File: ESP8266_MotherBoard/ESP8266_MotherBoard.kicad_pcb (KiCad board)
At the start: 2 copper layers, 67 parts, among them CN1 DIP-BLACK-FEMALE-HEADER-VERT_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, IC1 ADXL345, J1 Screw_Terminal_01x03, J10 Screw_Terminal_01x06, J11 Screw_Terminal_01x12, J2 DIP-BLACK-MALE-HEADER-VERT_4P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, J3 Screw_Terminal_01x02, J5 DIP-BLACK-MALE-HEADER-R_A_3P-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, J6 Screw_Terminal_01x02, J7 DIP-BLACK-MALE-HEADER-R_A_3P-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

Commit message: test branch sch and board changed
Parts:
- removed D5: 1N4001, OPL_Discrete_Semiconductor:DO-41
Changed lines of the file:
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@@
     (tracks 0)
     (zones 0)
-    (modules 67)
+    (modules 66)
     (nets 91)
   )
@@
       (net 38 GND))
   )
-  (module OPL_Discrete_Semiconductor:DO-41 (layer F.Cu)
-    (at 254 184.15 180)
-    (attr virtual)
-    (fp_text reference D5 (at 0 -2.286 180) (layer F.SilkS)
-      (effects (font (size 1 1) (thickness 0.15)))
-    )
-    (fp_text value 1N4001 (at 0 2.275 180) (layer F.Fab)
-      (effects (font (size 1 1) (thickness 0.15)))
-    )
-    (fp_line (start -2.54 -1.27) (end 2.54 -1.27) (layer F.SilkS) (width 0.127))
-    (fp_line (start -2.54 1.27) (end -2.54 -1.27) (layer F.SilkS) (width 0.127))
-    (fp_line (start 2.54 1.27) (end -2.54 1.27) (layer F.SilkS) (width 0.127))
-    (fp_line (start 2.54 -1.27) (end 2.54 1.27) (layer F.SilkS) (width 0.127))
-    (fp_line (start 2.54 0.3175) (end 2.54 -0.3175) (layer F.SilkS) (width 0.06604))
-    (fp_line (start 2.54 -0.3175) (end 3.29946 -0.3175) (layer F.SilkS) (width 0.06604))
-    (fp_line (start 3.29946 0.3175) (end 3.29946 -0.3175) (layer F.SilkS) (width 0.06604))
-    (fp_line (start 2.54 0.3175) (end 3.29946 0.3175) (layer F.SilkS) (width 0.06604))
-    (fp_line (start -3.29946 0.3175) (end -3.29946 -0.3175) (layer F.SilkS) (width 0.06604))
-    (fp_line (start -3.29946 -0.3175) (end -2.54 -0.3175) (layer F.SilkS) (width 0.06604))
-    (fp_line (start -2.54 0.3175) (end -2.54 -0.3175) (layer F.SilkS) (width 0.06604))
-    (fp_line (start -3.29946 0.3175) (end -2.54 0.3175) (layer F.SilkS) (width 0.06604))
-    (fp_line (start 1.27 1.27) (end 1.27 -1.27) (layer F.SilkS) (width 0.06604))
-    (fp_line (start 1.27 -1.27) (end 1.905 -1.27) (layer F.SilkS) (width 0.06604))
-    (fp_line (start 1.905 1.27) (end 1.905 -1.27) (layer F.SilkS) (width 0.06604))
-    (fp_line (start 1.27 1.27) (end 1.905 1.27) (layer F.SilkS) (width 0.06604))
-    (fp_line (start -2.325 -1) (end 2.325 -1) (layer F.Fab) (width 0.1))
-    (fp_line (start 2.325 -1) (end 2.325 1) (layer F.Fab) (width 0.1))
-    (fp_line (start 2.325 1) (end -2.325 1) (layer F.Fab) (width 0.1))
-    (fp_line (start -2.325 1) (end -2.325 -1) (layer F.Fab) (width 0.1))
-    (fp_line (start 5.65 -1.2) (end -5.65 -1.2) (layer F.CrtYd) (width 0.05))
-    (fp_line (start -5.65 -1.2) (end -5.65 1.2) (layer F.CrtYd) (width 0.05))
-    (fp_line (start -5.65 1.2) (end 5.65 1.2) (layer F.CrtYd) (width 0.05))
-    (fp_line (start 5.65 1.2) (end 5.65 -1.2) (layer F.CrtYd) (width 0.05))
-    (fp_text user %R (at 0 0 180) (layer F.Fab)
-      (effects (font (size 1 1) (thickness 0.15)))
-    )
-    (pad 2 thru_hole circle (at 4.445 0 180) (size 1.905 1.905) (drill 1.0414) (layers *.Cu *.Mask)
-      (net 38 GND))
-    (pad 1 thru_hole circle (at -4.445 0 180) (size 1.905 1.905) (drill 1.0414) (layers *.Cu *.Mask)
-      (net 36 PWM__toLoad_1))
-  )
   (module OPL_Discrete_Semiconductor:SOT-23 (layer F.Cu)

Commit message: added D3 ro PWM modul
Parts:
- added D3: 1N4001, OPL_Discrete_Semiconductor:DO-41, F.Cu at (250.2, 184.8)
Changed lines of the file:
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@@
     (tracks 0)
     (zones 0)
-    (modules 66)
+    (modules 67)
     (nets 91)
   )
@@
     )
   )
+  (module OPL_Discrete_Semiconductor:DO-41 (layer F.Cu)
+    (at 250.19 184.785)
+    (attr virtual)
+    (fp_text reference D3 (at 0 -2.286) (layer F.SilkS)
+      (effects (font (size 1 1) (thickness 0.15)))
+    )
+    (fp_text value 1N4001 (at 0 2.275) (layer F.Fab)
+      (effects (font (size 1 1) (thickness 0.15)))
+    )
+    (fp_line (start -2.54 -1.27) (end 2.54 -1.27) (layer F.SilkS) (width 0.127))
+    (fp_line (start -2.54 1.27) (end -2.54 -1.27) (layer F.SilkS) (width 0.127))
+    (fp_line (start 2.54 1.27) (end -2.54 1.27) (layer F.SilkS) (width 0.127))
+    (fp_line (start 2.54 -1.27) (end 2.54 1.27) (layer F.SilkS) (width 0.127))
+    (fp_line (start 2.54 0.3175) (end 2.54 -0.3175) (layer F.SilkS) (width 0.06604))
+    (fp_line (start 2.54 -0.3175) (end 3.29946 -0.3175) (layer F.SilkS) (width 0.06604))
+    (fp_line (start 3.29946 0.3175) (end 3.29946 -0.3175) (layer F.SilkS) (width 0.06604))
+    (fp_line (start 2.54 0.3175) (end 3.29946 0.3175) (layer F.SilkS) (width 0.06604))
+    (fp_line (start -3.29946 0.3175) (end -3.29946 -0.3175) (layer F.SilkS) (width 0.06604))
+    (fp_line (start -3.29946 -0.3175) (end -2.54 -0.3175) (layer F.SilkS) (width 0.06604))
+    (fp_line (start -2.54 0.3175) (end -2.54 -0.3175) (layer F.SilkS) (width 0.06604))
+    (fp_line (start -3.29946 0.3175) (end -2.54 0.3175) (layer F.SilkS) (width 0.06604))
+    (fp_line (start 1.27 1.27) (end 1.27 -1.27) (layer F.SilkS) (width 0.06604))
+    (fp_line (start 1.27 -1.27) (end 1.905 -1.27) (layer F.SilkS) (width 0.06604))
+    (fp_line (start 1.905 1.27) (end 1.905 -1.27) (layer F.SilkS) (width 0.06604))
+    (fp_line (start 1.27 1.27) (end 1.905 1.27) (layer F.SilkS) (width 0.06604))
+    (fp_line (start -2.325 -1) (end 2.325 -1) (layer F.Fab) (width 0.1))
+    (fp_line (start 2.325 -1) (end 2.325 1) (layer F.Fab) (width 0.1))
+    (fp_line (start 2.325 1) (end -2.325 1) (layer F.Fab) (width 0.1))
+    (fp_line (start -2.325 1) (end -2.325 -1) (layer F.Fab) (width 0.1))
+    (fp_line (start 5.65 -1.2) (end -5.65 -1.2) (layer F.CrtYd) (width 0.05))
+    (fp_line (start -5.65 -1.2) (end -5.65 1.2) (layer F.CrtYd) (width 0.05))
+    (fp_line (start -5.65 1.2) (end 5.65 1.2) (layer F.CrtYd) (width 0.05))
+    (fp_line (start 5.65 1.2) (end 5.65 -1.2) (layer F.CrtYd) (width 0.05))
+    (fp_text user %R (at 0 0) (layer F.Fab)
+      (effects (font (size 1 1) (thickness 0.15)))
+    )
+    (pad 2 thru_hole circle (at 4.445 0) (size 1.905 1.905) (drill 1.0414) (layers *.Cu *.Mask)
+      (net 38 GND))
+    (pad 1 thru_hole circle (at -4.445 0) (size 1.905 1.905) (drill 1.0414) (layers *.Cu *.Mask)
+      (net 36 PWM__toLoad_1))
+  )
 )

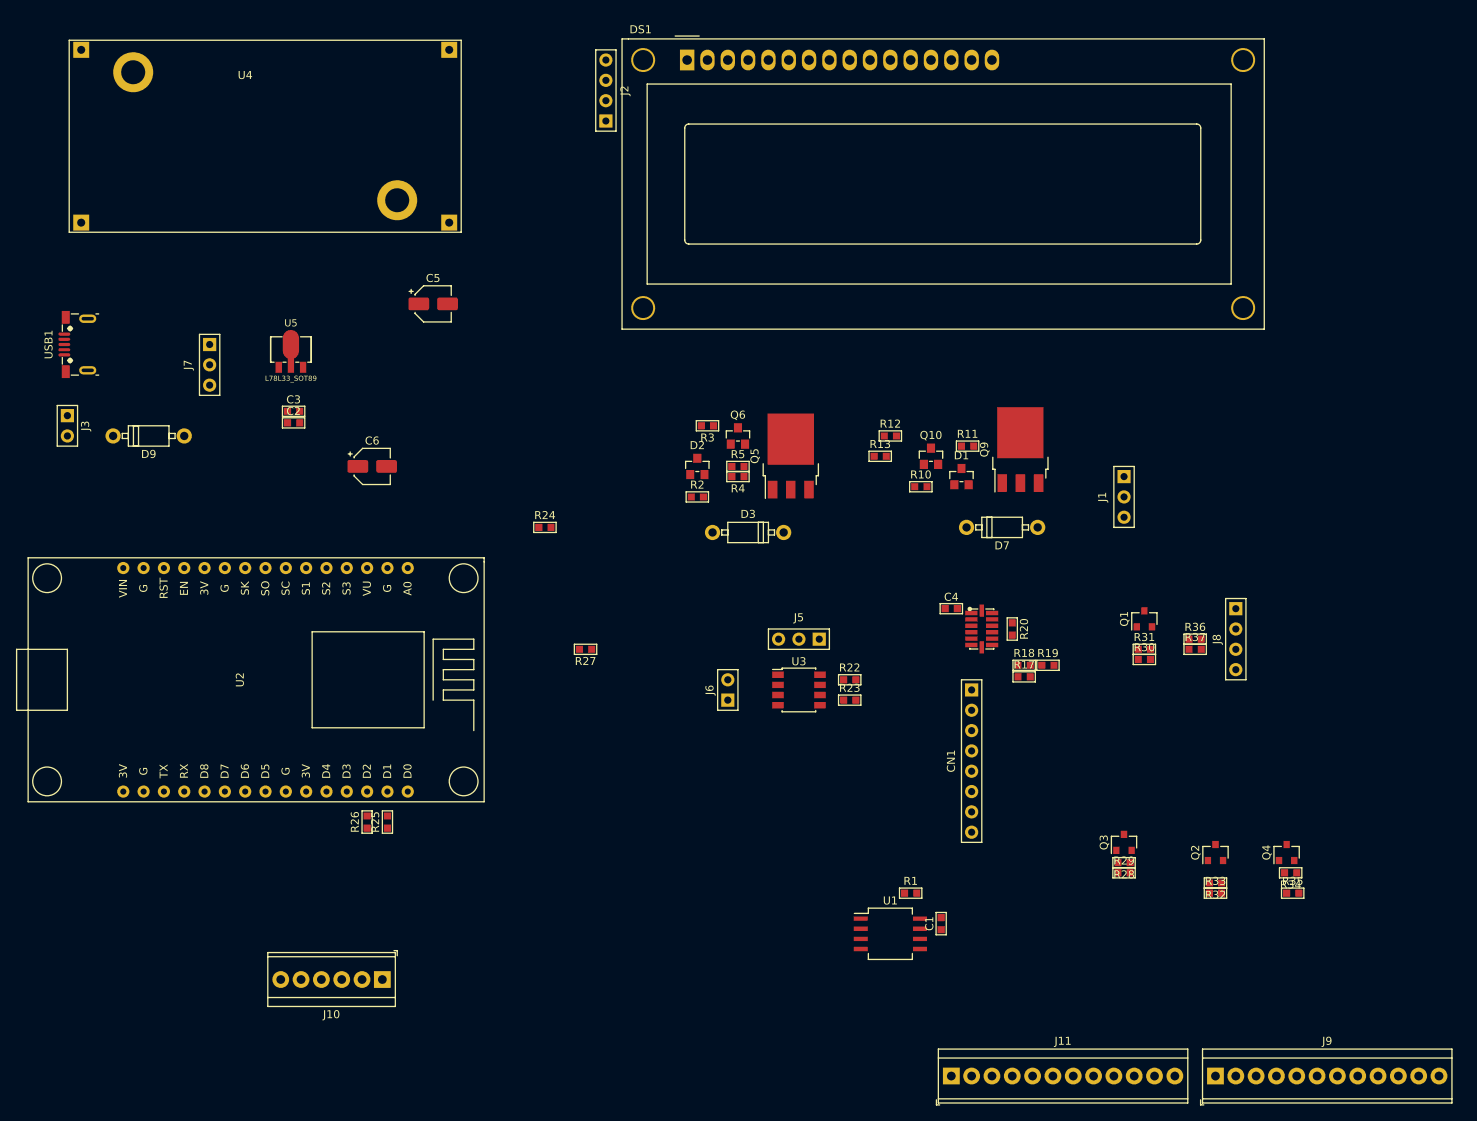
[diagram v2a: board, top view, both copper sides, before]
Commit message: pwm module corrections and simulations LTS
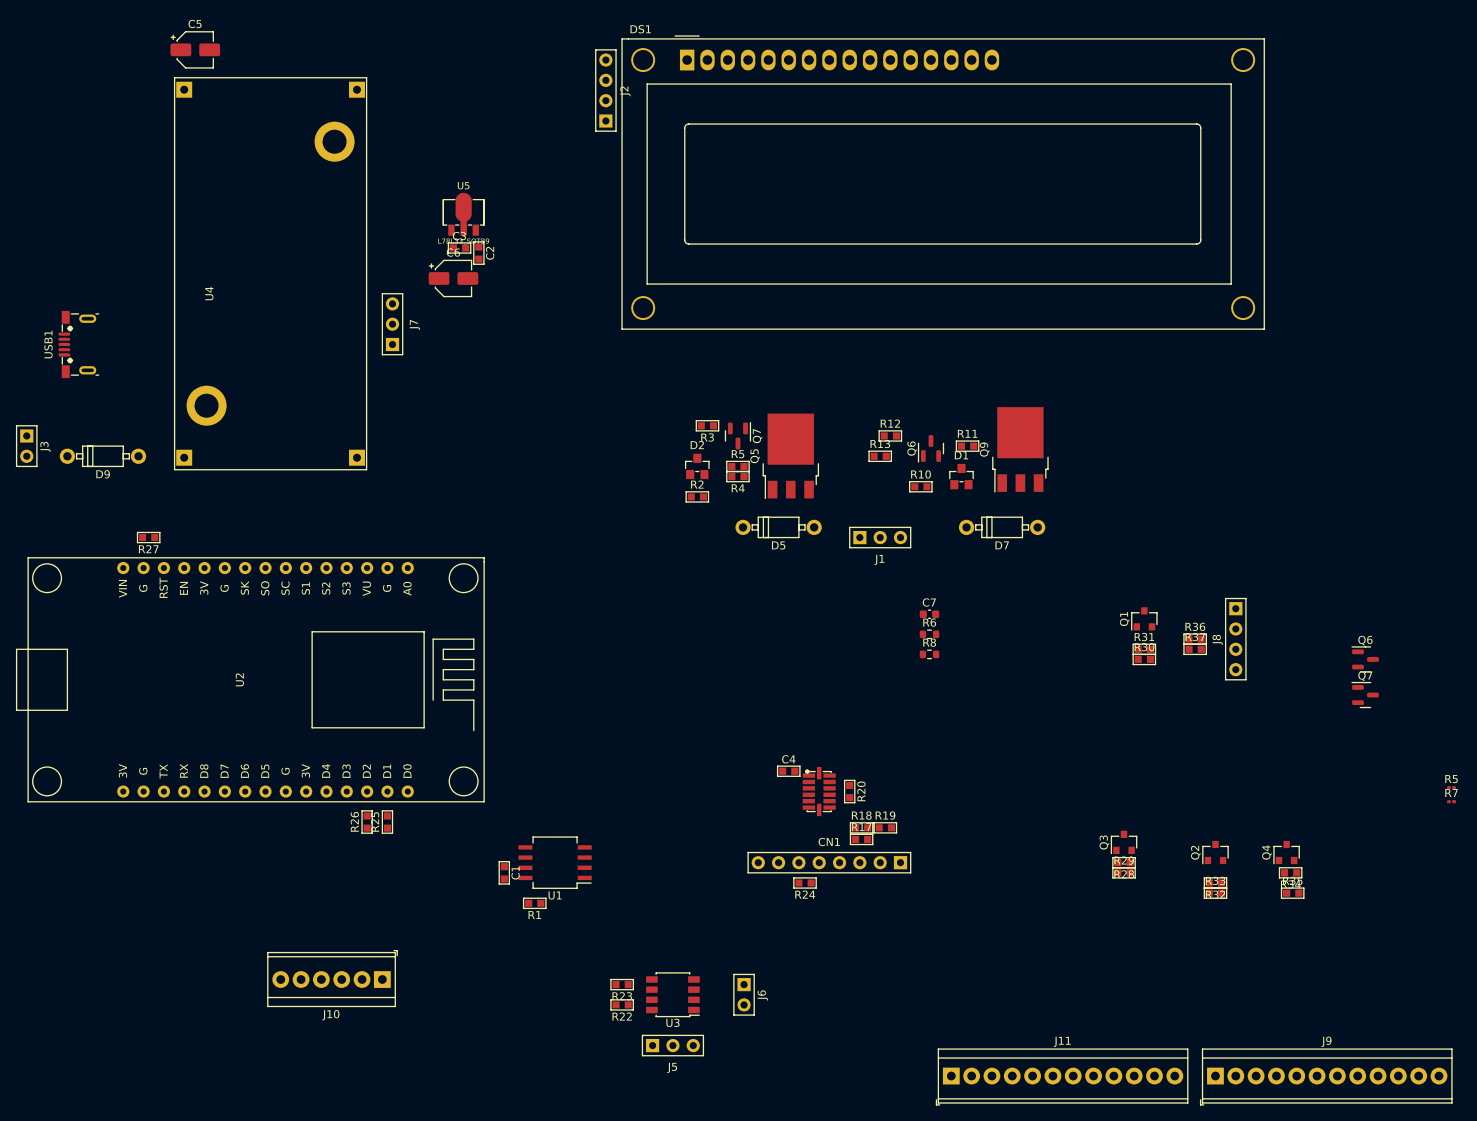
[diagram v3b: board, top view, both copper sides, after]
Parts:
- removed D3: 1N4001, OPL_Discrete_Semiconductor:DO-41
- removed Q10: MMBT2222, OPL_Discrete_Semiconductor:SOT-23
- removed the Q6 at (248.9, 172.7)
- added C7: CERAMIC-100NF-50V-10%-X7R_0603_, Capacitor_SMD:C_0603_1608Metric, F.Cu at (272.9, 195.0)
- added D5: 1N4001, OPL_Discrete_Semiconductor:DO-41, F.Cu at (254.0, 184.2)
- added Q6: MMBT2907, Package_TO_SOT_SMD:SOT-23, F.Cu at (273.1, 174.3)
- added Q6: BC849, Package_TO_SOT_SMD:SOT-23, F.Cu at (327.4, 200.7)
- added Q7: MMBT2907, Package_TO_SOT_SMD:SOT-23, F.Cu at (248.9, 172.7)
- added Q7: BC849, Package_TO_SOT_SMD:SOT-23, F.Cu at (327.4, 205.1)
- added R5: SMD-RES-10K-1%-1_10W_0603_, Resistor_SMD:R_0201_0603Metric, F.Cu at (338.1, 216.7)
- added R6: OPL_Resistor_SMD-RES-2.2K-5%-1_10W_0603_, Resistor_SMD:R_0603_1608Metric, F.Cu at (272.9, 197.5)
- added R7: SMD-RES-10K-1%-1_10W_0603_, Resistor_SMD:R_0201_0603Metric, F.Cu at (338.1, 218.4)
- added R8: OPL_Resistor_SMD-RES-2.2K-5%-1_10W_0603_, Resistor_SMD:R_0603_1608Metric, F.Cu at (272.9, 200.0)
- D1, D2: value BZX84C24BS -> BZX84C15BS
- Q5, Q9: value Q_PMOS_GDS -> IRF9630
- R10, R2: value SMD-RES-2.2K-5%-1_10W_0603_ -> SMD-RES-10K-5%-1_10W_0603_
- R11, R3: value SMD-RES-100R-5%-1_10W_0603_ -> SMD-RES-1k5-5%-1_10W_0603_
- R28: value SMD-RES-10K-1%-1_10W_0603_ -> 10k
- moved R27 56.4 mm to (175.3, 185.4)
- moved R24 55.1 mm to (257.3, 228.6), turned to 180 degrees
- moved C1 55.0 mm to (219.7, 227.3), turned to -90 degrees
- moved J5 53.2 mm to (240.8, 248.9), turned to 180 degrees
- moved R22 49.6 mm to (234.4, 243.8), turned to 180 degrees
- moved R1 47.0 mm to (223.5, 231.1), turned to 180 degrees
- moved R23 45.5 mm to (234.4, 241.3), turned to 180 degrees
- moved C5 43.5 mm to (181.1, 124.5)
- moved U1 42.8 mm to (226.1, 226.1), turned to 180 degrees
- moved U3 41.2 mm to (240.8, 242.6), turned to 180 degrees
- moved J6 38.2 mm to (249.7, 242.6), turned to -90 degrees
- moved C2 31.4 mm to (216.5, 149.9), turned to -90 degrees
- moved J1 30.9 mm to (266.7, 185.4), turned to 180 degrees
- moved C3 29.1 mm to (214.1, 149.2)
- moved R18 28.7 mm to (264.4, 221.7)
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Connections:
- CN1 pad 3: Net-(CN1-Pad3) -> unconnected-(CN1-Pad3)
- CN1 pad 4: Net-(CN1-Pad4) -> unconnected-(CN1-Pad4)
- CN1 pad 5: Net-(CN1-Pad5) -> unconnected-(CN1-Pad5)
- D1 pad 1: +5V -> +12V
- DS1 pad 1: Net-(DS1-Pad1) -> unconnected-(DS1-VSS-Pad1)
- DS1 pad 10: Net-(DS1-Pad10) -> unconnected-(DS1-D3-Pad10)
- DS1 pad 11: Net-(DS1-Pad11) -> unconnected-(DS1-D4-Pad11)
- DS1 pad 12: Net-(DS1-Pad12) -> unconnected-(DS1-D5-Pad12)
- DS1 pad 13: Net-(DS1-Pad13) -> unconnected-(DS1-D6-Pad13)
- DS1 pad 14: Net-(DS1-Pad14) -> unconnected-(DS1-D7-Pad14)
- DS1 pad 15: Net-(DS1-Pad15) -> unconnected-(DS1-LED(+)-Pad15)
- DS1 pad 16: Net-(DS1-Pad16) -> unconnected-(DS1-LED(-)-Pad16)
- DS1 pad 2: Net-(DS1-Pad2) -> unconnected-(DS1-VDD-Pad2)
- DS1 pad 3: Net-(DS1-Pad3) -> unconnected-(DS1-VO-Pad3)
- DS1 pad 4: Net-(DS1-Pad4) -> unconnected-(DS1-RS-Pad4)
- DS1 pad 5: Net-(DS1-Pad5) -> unconnected-(DS1-R/W-Pad5)
- DS1 pad 6: Net-(DS1-Pad6) -> unconnected-(DS1-E-Pad6)
- DS1 pad 7: Net-(DS1-Pad7) -> unconnected-(DS1-D0-Pad7)
- DS1 pad 8: Net-(DS1-Pad8) -> unconnected-(DS1-D1-Pad8)
- DS1 pad 9: Net-(DS1-Pad9) -> unconnected-(DS1-D2-Pad9)
- IC1 pad 10: Net-(IC1-Pad10) -> unconnected-(IC1-NC-Pad10)
- IC1 pad 11: Net-(IC1-Pad11) -> unconnected-(IC1-NC-Pad11)
- IC1 pad 3: Net-(IC1-Pad3) -> unconnected-(IC1-NC-Pad3)
- J11 pad 12: Net-(J11-Pad12) -> unconnected-(J11-Pin_12-Pad12)
- Q2 pad 2: +5V -> +3V3
- Q3 pad 2: +5V -> +3V3
- Q4 pad 2: +5V -> +3V3
- Q5 pad 2: +12V -> PWM__toLoad_1
- Q5 pad 3: PWM__toLoad_1 -> +12V
- Q9 pad 2: +5V -> PWM__toLoad_2
- Q9 pad 3: PWM__toLoad_2 -> +12V
- R10 pad 1: +5V -> +12V
- R13 pad 1: +5V -> +12V
- R25 pad 1: +5V -> +3V3
- R26 pad 1: +5V -> +3V3
- R27 pad 2: +5V -> +3V3
- R28 pad 1: +5V -> +3V3
- R31 pad 2: MCU_GPO_3 -> MCU_GPO_4
- R32 pad 1: +5V -> +3V3
- R34 pad 1: +5V -> +3V3
- R5 pad 1: +5V -> +12V
- U2 pad 11: Net-(U2-Pad11) -> unconnected-(U2-3.3V-Pad11)
- U2 pad 16: Net-(U2-Pad16) -> unconnected-(U2-3.3V-Pad16)
- U2 pad 2: Net-(U2-Pad2) -> unconnected-(U2-RSV-Pad2)
- U2 pad 25: Net-(U2-Pad25) -> unconnected-(U2-3.3V-Pad25)
- U2 pad 3: Net-(U2-Pad3) -> unconnected-(U2-RSV-Pad3)
- USB1 pad 2: Net-(USB1-Pad2) -> unconnected-(USB1-DM-Pad2)
- USB1 pad 3: Net-(USB1-Pad3) -> unconnected-(USB1-DP-Pad3)
- USB1 pad 4: Net-(USB1-Pad4) -> unconnected-(USB1-ID-Pad4)
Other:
- net class Default removed
